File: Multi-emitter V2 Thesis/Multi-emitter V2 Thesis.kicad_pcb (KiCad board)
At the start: 2 copper layers, 83 x 41 mm, 45 parts, among them J0 DA15_Pins, J1 Emitter Input, J2 Emitter Input, J3 Emitter Input, J4 Emitter Input, J5 Emitter Input, J6 Emitter Input, J7 Emitter Input, J8 Emitter Input, Q1 NMOS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

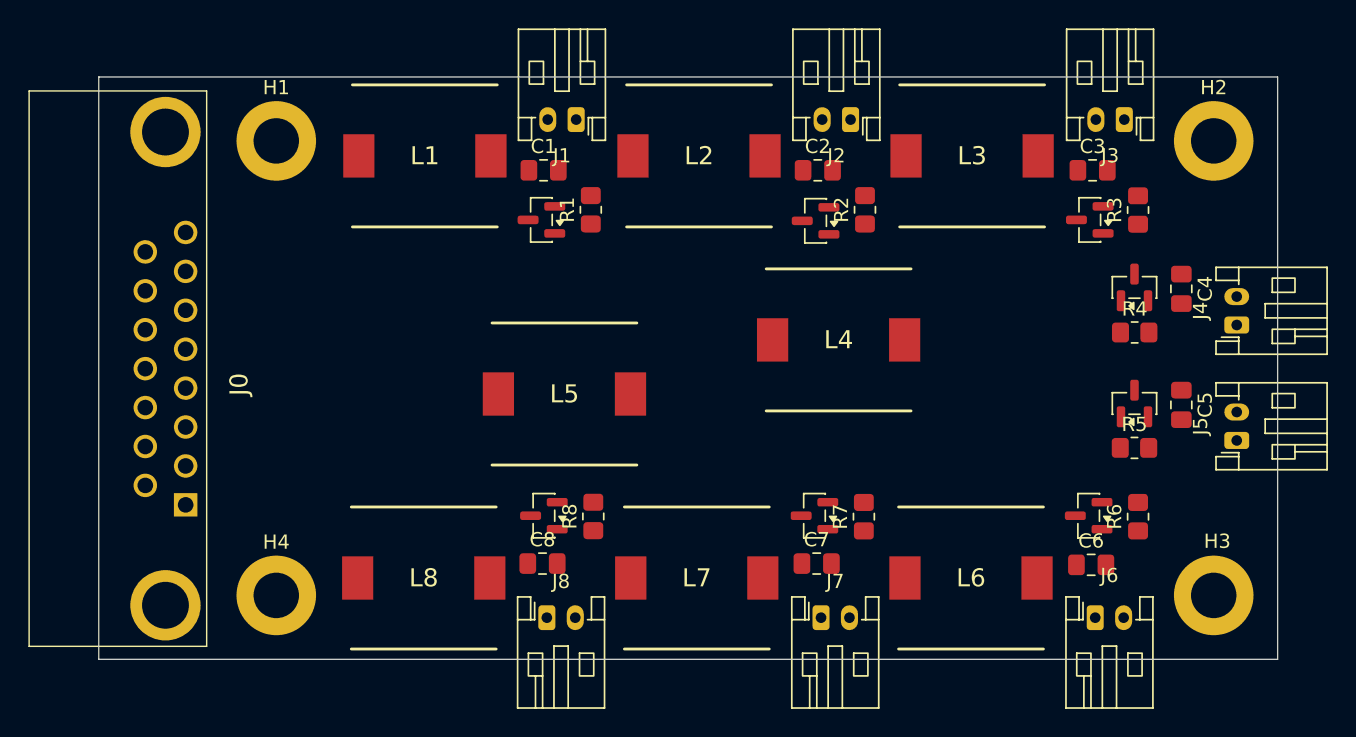
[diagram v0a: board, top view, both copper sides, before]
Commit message: PCB layout done on emitter PCB - ready to order
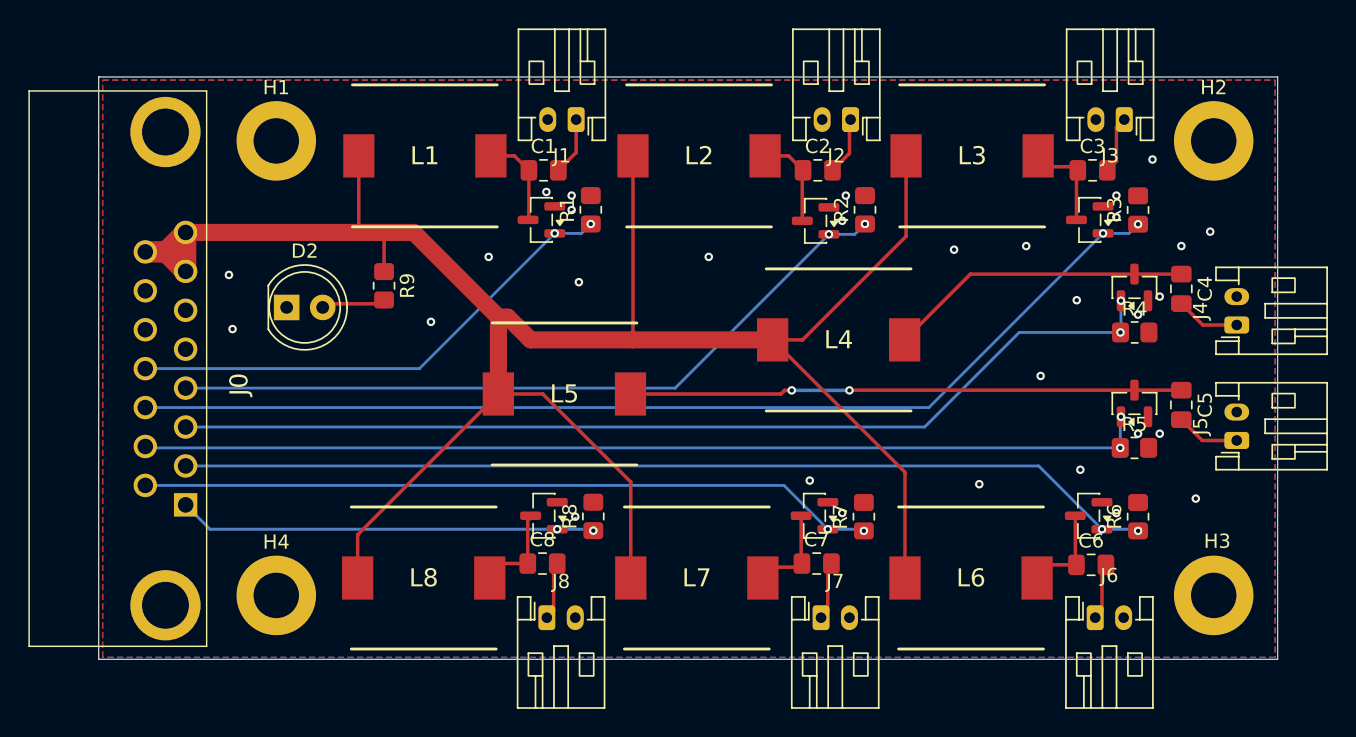
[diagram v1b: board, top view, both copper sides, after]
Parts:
- added D2: LED, LED_THT:LED_D5.0mm, F.Cu at (125.7, 77.7)
- added R9: 1k, Resistor_SMD:R_0805_2012Metric_Pad1.20x1.40mm_HandSolder, F.Cu at (132.6, 76.2)
- moved C5 46.3 mm to (188.7, 84.6), turned to -90 degrees
- moved C8 46.3 mm to (143.7, 95.8), turned to 0 degrees
- moved C6 19.3 mm to (182.4, 95.8)
- moved C7 19.3 mm to (163.0, 95.8)
- renumbered C8 to C5, C7 to C6, C6 to C7, C5 to C8
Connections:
- R7 pad 1: unconnected-(R7-Pad1) -> /PWM7
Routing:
- net VCC: track 0.00 -> 153.7 mm
- net /PWM3: track 0.00 -> 75.2 mm, vias 0 -> 2
- net /PWM5: track 0.00 -> 70.9 mm, vias 0 -> 2
- net /PWM4: track 0.00 -> 70.8 mm, vias 0 -> 2
- net /PWM6: track 0.00 -> 68.9 mm, vias 0 -> 2
- net /PWM2: track 0.00 -> 52.6 mm, vias 0 -> 2
- net /PWM7: track 0.00 -> 51.9 mm, vias 0 -> 2
- net Net-(Q5-D): track 0.00 -> 38.9 mm, vias 0 -> 2
- net /PWM1: track 0.00 -> 35.6 mm, vias 0 -> 2
- net /PWM8: track 0.00 -> 29.5 mm, vias 0 -> 2
- net Net-(Q4-D): track 0.00 -> 21.4 mm
- net Net-(Q8-D): track 0.00 -> 8.06 mm
- net Net-(Q3-D): track 0.00 -> 6.75 mm
- net Net-(Q2-D): track 0.00 -> 6.67 mm
- net Net-(Q6-D): track 0.00 -> 6.65 mm
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- added copper zone on B.Cu, net GND
- added copper zone on F.Cu, net GND

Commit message: Added some fancy silkscreen text and generated gerber files
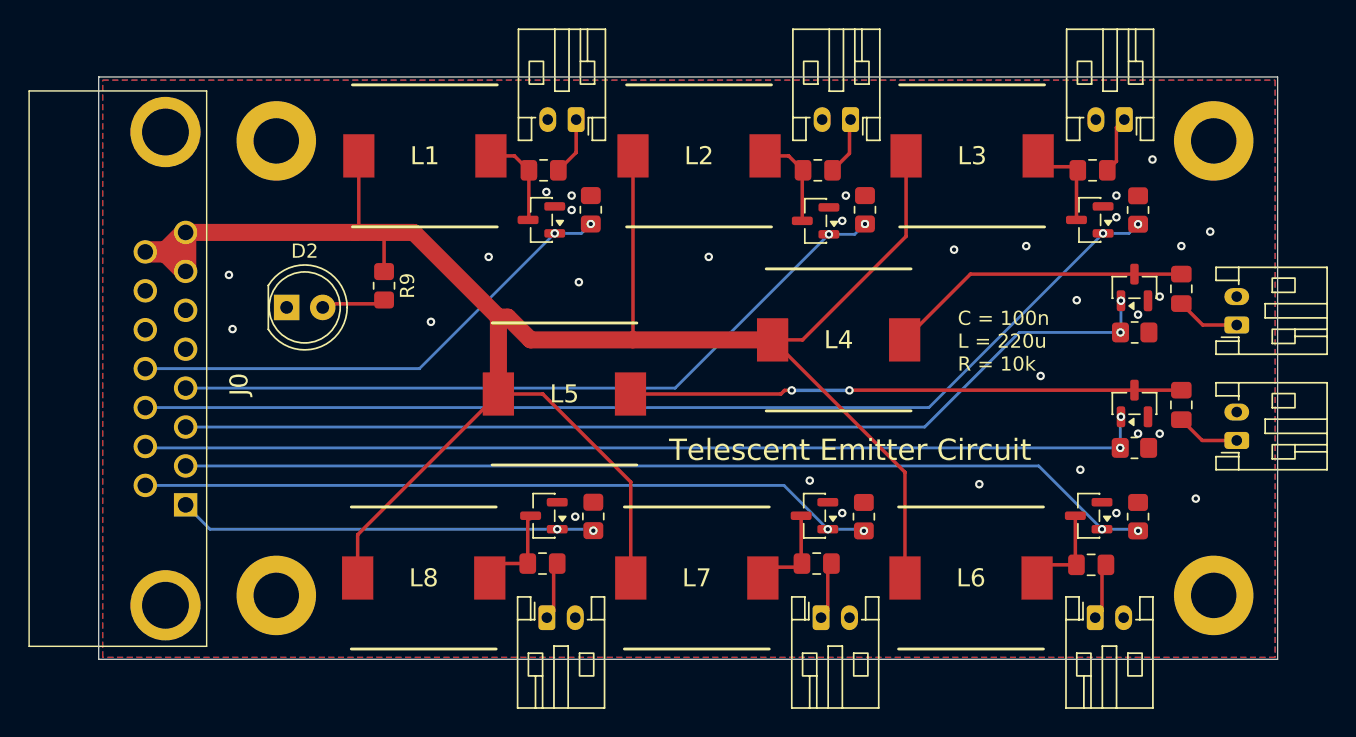
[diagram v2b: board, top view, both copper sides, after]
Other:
- board text added: "C = 100n L = 220u R = 10k"
- board text added: "Telescent Emitter Circuit"
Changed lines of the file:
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@@
 			(sketchdnponfab yes)
 			(crossoutdnponfab yes)
-			(subtractmaskfromsilk no)
+			(subtractmaskfromsilk yes)
 			(outputformat 1)
 			(mirror no)
-			(drillshape 1)
+			(drillshape 0)
 			(scaleselection 1)
 			(outputdirectory "")
@@
 			(at 0 -1.65 90)
 			(layer "F.SilkS")
+			(hide yes)
 			(effects
 				(font
@@
 			(at 0 1.65 90)
 			(layer "F.Fab")
+			(hide yes)
 			(effects
 				(font
@@
 			(at 0 -1.68 0)
 			(layer "F.SilkS")
+			(hide yes)
 			(effects
 				(font
@@
 			(at 0 1.68 0)
 			(layer "F.Fab")
+			(hide yes)
 			(effects
 				(font
@@
 			(at 1 -2.55 0)
 			(layer "F.SilkS")
+			(hide yes)
 			(effects
 				(font
@@
 			(at 1 -2.55 0)
 			(layer "F.SilkS")
+			(hide yes)
 			(effects
 				(font
@@
 			(at 0 -3.75 0)
 			(layer "F.SilkS")
+			(hide yes)
 			(effects
 				(font
@@
 			(at 1 -2.55 90)
 			(layer "F.SilkS")
+			(hide yes)
 			(effects
 				(font
@@
 			(at 1 -2.55 0)
 			(layer "F.SilkS")
+			(hide yes)
 			(effects
 				(font
@@
 			(at 0 -1.65 90)
 			(layer "F.SilkS")
+			(hide yes)
 			(effects
 				(font
@@
 			(at 0 1.65 90)
 			(layer "F.Fab")
+			(hide yes)
 			(effects
 				(font
@@
 			(at 0 -1.65 0)
 			(layer "F.SilkS")
+			(hide yes)
 			(effects
 				(font
@@
 			(at 0 -3.75 0)
 			(layer "F.SilkS")
+			(hide yes)
 			(effects
 				(font
@@
 			(at 0 -1.65 90)
 			(layer "F.SilkS")
+			(hide yes)
 			(effects
 				(font
@@
 			(at 0 1.65 90)
 			(layer "F.Fab")
+			(hide yes)
 			(effects
 				(font
@@
 			(at 0 -1.68 270)
 			(layer "F.SilkS")
+			(hide yes)
 			(effects
 				(font
@@
 			(at 0 1.68 270)
 			(layer "F.Fab")
+			(hide yes)
 			(effects
 				(font
@@
 			(at 0 -1.65 90)
 			(layer "F.SilkS")
+			(hide yes)
 			(effects
 				(font
@@
 			(at 0 1.65 90)
 			(layer "F.Fab")
+			(hide yes)
 			(effects
 				(font
@@
 			(at 0 -1.68 0)
 			(layer "F.SilkS")
+			(hide yes)
 			(effects
 				(font
@@
 			(at 0 1.68 0)
 			(layer "F.Fab")
+			(hide yes)
 			(effects
 				(font
@@
 			(at 1 -2.55 0)
 			(layer "F.SilkS")
+			(hide yes)
 			(effects
 				(font
@@
 			(at 1 -2.968 0)
 			(layer "F.SilkS")
+			(hide yes)
 			(effects
 				(font
@@
 			(at 0 -1.65 0)
 			(layer "F.SilkS")
+			(hide yes)
 			(effects
 				(font
@@
 			(at 0 -1.68 0)
 			(layer "F.SilkS")
+			(hide yes)
 			(effects
 				(font
@@
 			(at 0 1.68 0)
 			(layer "F.Fab")
+			(hide yes)
 			(effects
 				(font
@@
 			(at 0 -1.65 90)
 			(layer "F.SilkS")
+			(hide yes)
 			(effects
 				(font
@@
 			(at 0 1.65 90)
 			(layer "F.Fab")
+			(hide yes)
 			(effects
 				(font
@@
 			(at 0 -1.68 0)
 			(layer "F.SilkS")
+			(hide yes)
 			(effects
 				(font
@@
 			(at 0 1.68 0)
 			(layer "F.Fab")
+			(hide yes)
 			(effects
 				(font
@@
 			(at 0 -3.75 0)
 			(layer "F.SilkS")
+			(hide yes)
 			(effects
 				(font
@@
 			(at 0 -1.68 0)
 			(layer "F.SilkS")
+			(hide yes)
 			(effects
 				(font
@@
 			(at 0 1.68 0)
 			(layer "F.Fab")
+			(hide yes)
 			(effects
 				(font
@@
 			(at 1 -2.55 0)
 			(layer "F.SilkS")
+			(hide yes)
 			(effects
 				(font
@@
 			(at 0 -1.68 90)
 			(layer "F.SilkS")
+			(hide yes)
 			(effects
 				(font
@@
 			(at 0 1.68 90)
 			(layer "F.Fab")
+			(hide yes)
 			(effects
 				(font
@@
 			(at 0.254 -3.81 0)
 			(layer "F.SilkS")
+			(hide yes)
 			(effects
 				(font
@@
 			(at 1 -2.55 90)
 			(layer "F.SilkS")
+			(hide yes)
 			(effects
 				(font
@@
 			(at 0 -1.68 180)
 			(layer "F.SilkS")
+			(hide yes)
 			(effects
 				(font
@@
 			(at 0 1.68 180)
 			(layer "F.Fab")
+			(hide yes)
 			(effects
 				(font
@@
 			(at 0 -1.65 90)
 			(layer "F.SilkS")
+			(hide yes)
 			(effects
 				(font
@@
 			(at 0 1.65 90)
 			(layer "F.Fab")
+			(hide yes)
 			(effects
 				(font
@@
 		(layer "Edge.Cuts")
 	)
+	(gr_text "Telescent Emitter Circuit"
+		(at 152.654 88.646 0)
+		(layer "F.SilkS")
+		(effects
+			(font
+				(size 1.5 1.5)
+				(thickness 0.125)
+			)
+			(justify left bottom)
+		)
+	)
+	(gr_text "C = 100n\nL = 220u\nR = 10k"
+		(at 172.974 82.296 0)
+		(layer "F.SilkS")
+		(effects
+			(font
+				(size 1 1)
+				(thickness 0.125)
+			)
+			(justify left bottom)
+		)
+	)
 	(segment
